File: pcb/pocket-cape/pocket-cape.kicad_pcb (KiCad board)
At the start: 2 copper layers, 49 x 32.1 mm, 29 parts, among them J1 Sync1, J10 Display, J11 USB1, J2 12..16V, J3 Sync2, J4 Sled, J5 Laser1, J6 PM1, J7 PM2, J8 Laser2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

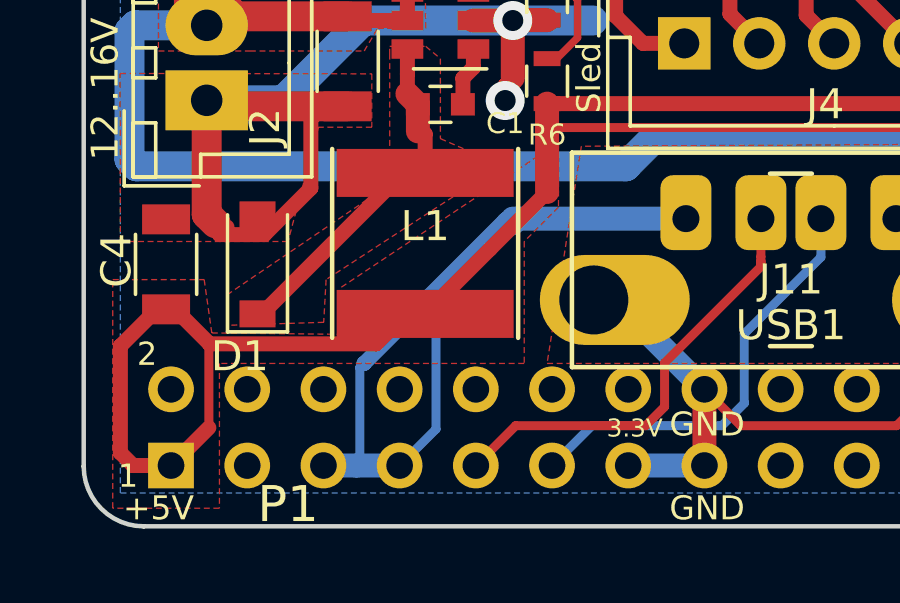
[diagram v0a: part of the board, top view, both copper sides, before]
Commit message: Update values in Schematic; directly connect USB 5V with DC/DC 5V.
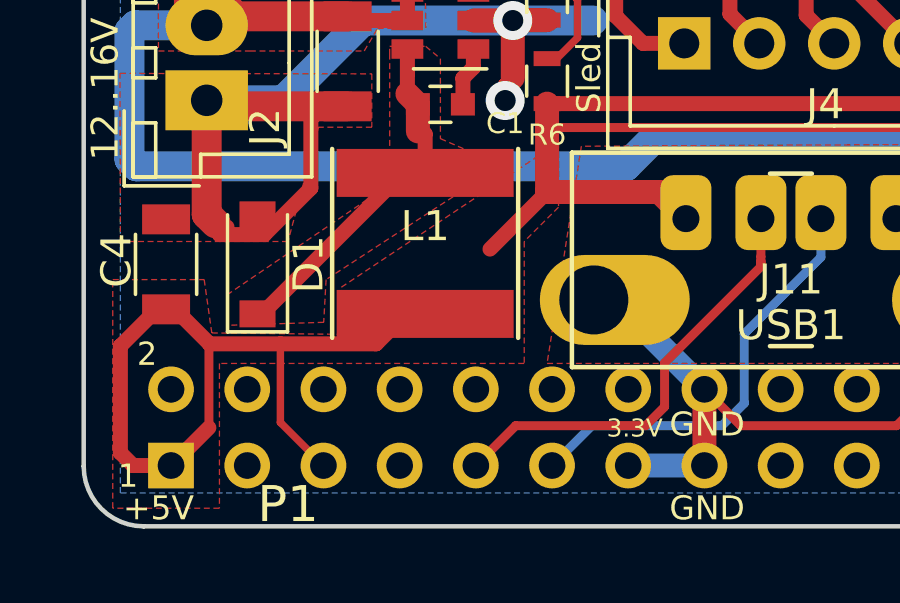
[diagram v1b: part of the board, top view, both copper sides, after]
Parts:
- D1: value D -> MBR230LSFT1G
- R6: value R -> 6k2
- R7: value R -> 1k2
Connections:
- J11 pad 1: USB_DC -> VDD_5V
- P1 pad 5: USB_DC -> VDD_5V
- P1 pad 7: USB_DC -> Net-(P1-Pad7)
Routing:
- net USB_DC: track 32.5 -> 0.00 mm
- net VDD_5V: track 83.8 -> 90.4 mm

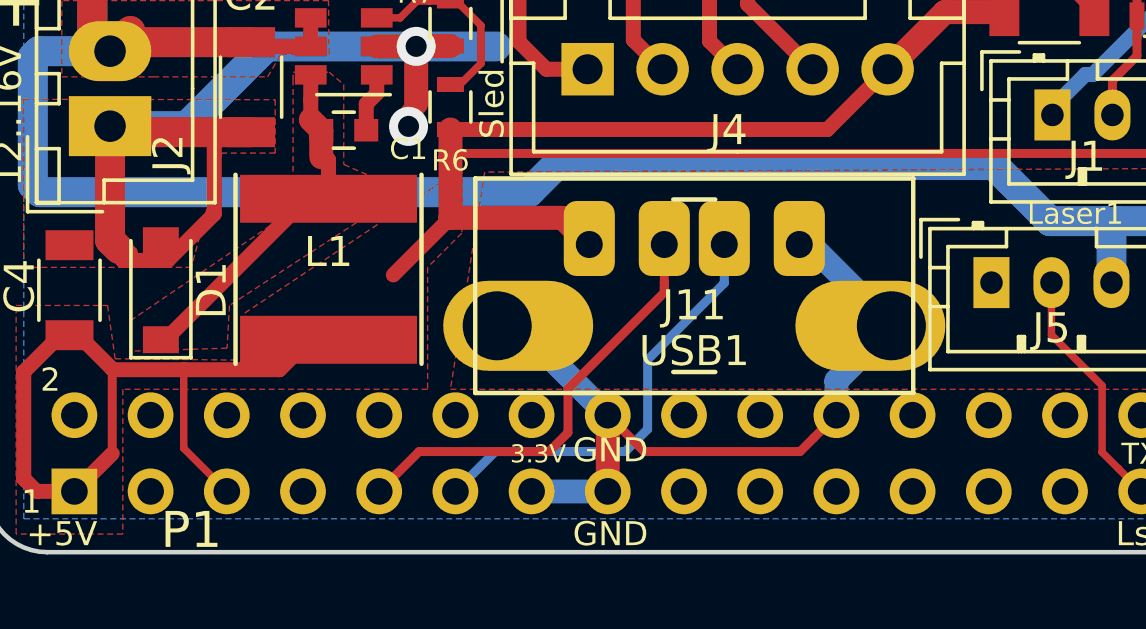
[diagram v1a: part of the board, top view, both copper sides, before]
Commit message: Connect USB output to SYS 5V
o SYS 5V has a cleaner switch-on transition than the raw DC/DC out.
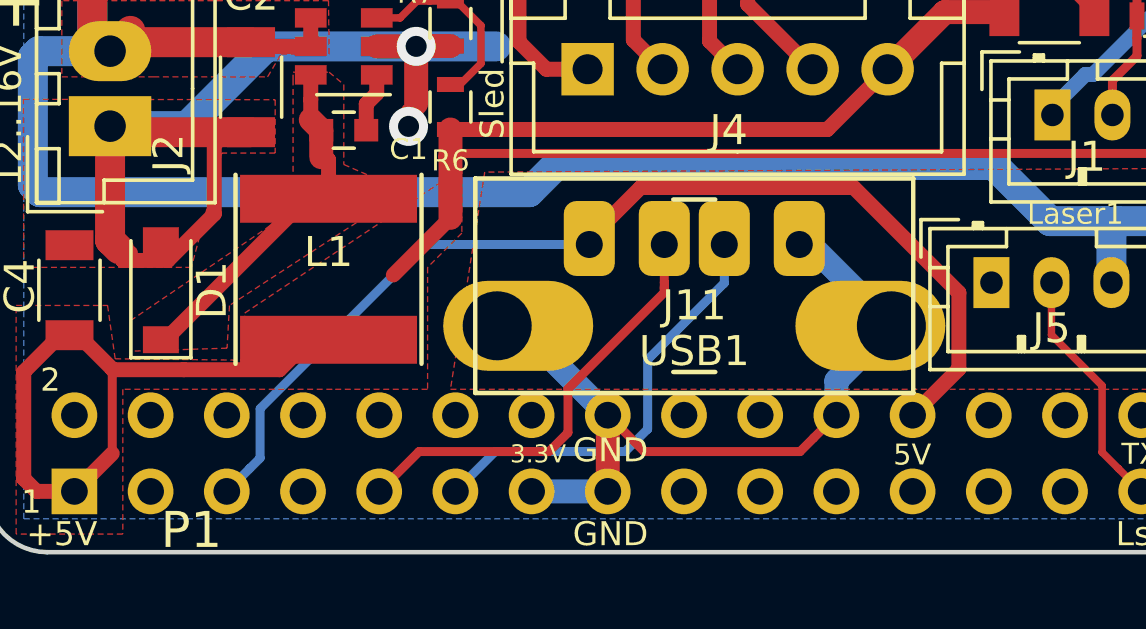
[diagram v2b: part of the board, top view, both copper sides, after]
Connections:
- J11 pad 1: VDD_5V -> SYS_VOUT
- P1 pad 24: Net-(P1-Pad24) -> SYS_VOUT
- P1 pad 5: VDD_5V -> SYS_VOUT
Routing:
- net SYS_VOUT: track 0.00 -> 35.8 mm
- net VDD_5V: track 90.4 -> 80.7 mm
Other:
- board text added: "5V"

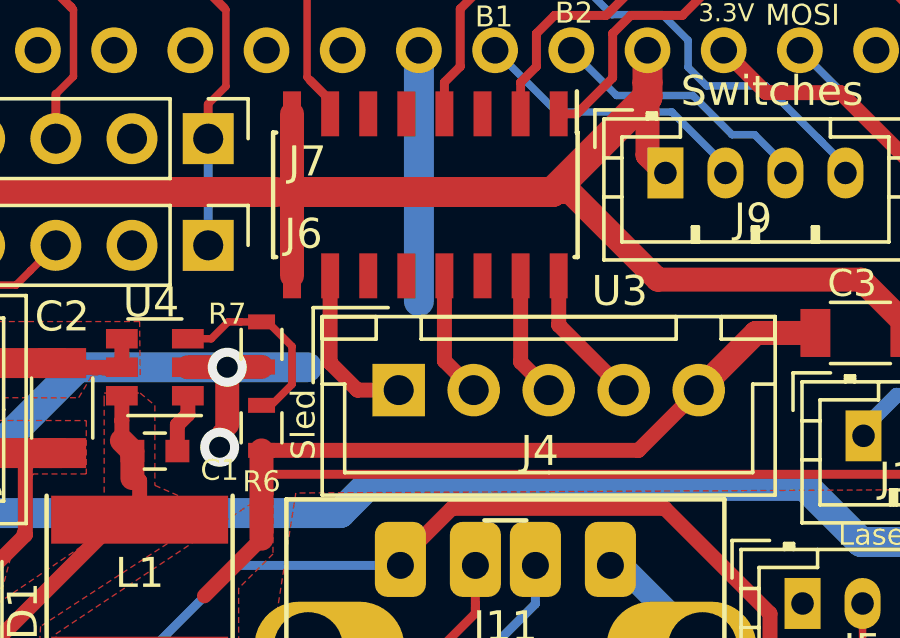
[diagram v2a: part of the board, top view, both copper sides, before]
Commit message: Connect flyback diodes to +5V.
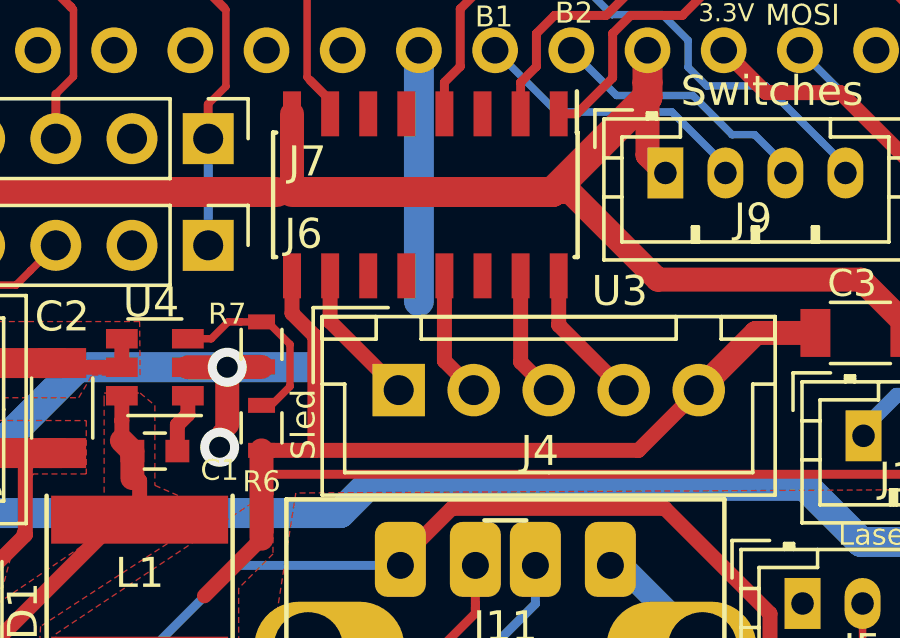
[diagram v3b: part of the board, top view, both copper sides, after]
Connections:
- U3 pad 9: GND -> VDD_5V
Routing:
- net VDD_5V: track 80.7 -> 86.9 mm
- net GND: track 145.7 -> 142.9 mm
- net Net-(J4-Pad1): track 5.56 -> 4.76 mm
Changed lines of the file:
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@@
-(kicad_pcb (version 20170922) (host pcbnew "(2017-10-06 revision d6c0d320d)-master")
+(kicad_pcb (version 20170922) (host pcbnew "(2017-10-26 revision fc5e8e5f5)-master")
 (general
   (thickness 1.6)
   (drawings 42)
-  (tracks 343)
-  (zones 0)
-  (modules 29)
-  (nets 86)
-)
-(page A4)
-(title_block
-  (title "LDGraphy PocketBeagle Cape")
-  (date 2017-09-30)
-  (comment 1 h.zeller@acm.org)
-  (comment 2 http://github.com/hzeller/ldgraphy)
-)
-(layers
-  (0 Top signal)
-  (31 Bottom signal)
-  (32 B.Adhes user hide)
-  (33 F.Adhes user hide)
-  (34 B.Paste user hide)
-  (35 F.Paste user hide)
-  (36 B.SilkS user)
-  (37 F.SilkS user)
-  (38 B.Mask user hide)
-  (39 F.Mask user hide)
-  (40 Dwgs.User user hide)
-  (41 Cmts.User user hide)
-  (42 Eco1.User user hide)
-  (43 Eco2.User user hide)
-  (44 Edge.Cuts user)
-  (45 Margin user hide)
-  (46 B.CrtYd user)
-  (47 F.CrtYd user)
-  (48 B.Fab user)
-  (49 F.Fab user)
-)
-(general
-  (thickness 1.6)
-  (drawings 42)
-  (tracks 343)
+  (tracks 345)
   (zones 0)
   (modules 29)
@@
 )
 (setup
-  (last_trace_width 0.25)
+  (last_trace_width 0.5)
   (user_trace_width 0.25)
   (user_trace_width 0.3)
@@
       (net 1 GND))
     (pad 9 smd rect (at 2.7 4.445 270) (size 1.5 0.6) (layers Top F.Paste F.Mask)
-      (net 1 GND))
+      (net 2 VDD_5V))
     (pad 10 smd rect (at 2.7 3.175 270) (size 1.5 0.6) (layers Top F.Paste F.Mask)
       (net 6 "Net-(J4-Pad1)"))
@@
   (segment (start 152.3111 116.4336) (end 152.3111 115.2869) (width 0.8) (layer Bottom) (net 1))
   (segment (start 152.3111 115.2869) (end 154.144 113.454) (width 0.8) (layer Bottom) (net 1))
-  (segment (start 140.462 98.298) (end 140.462 101.092) (width 0.8) (layer Top) (net 1))
   (segment (start 140.462 95.692) (end 140.462 98.298) (width 0.8) (layer Top) (net 1))
   (segment (start 140.462 98.298) (end 149.146002 98.298) (width 1) (layer Top) (net 1))
@@
   (segment (start 168.77 97.2775) (end 168.77 96.71) (width 0.25) (layer Top) (net 1))
   (segment (start 144.812 116.3127) (end 144.6911 116.4336) (width 0.8) (layer Top) (net 1))
+  (segment (start 141.224 106.91) (end 152.01 106.91) (width 0.5) (layer Top) (net 2))
+  (segment (start 139.446 106.91) (end 141.224 106.91) (width 0.5) (layer Top) (net 2))
+  (segment (start 140.462 101.092) (end 140.462 102.342) (width 0.5) (layer Top) (net 2))
+  (segment (start 140.462 102.342) (end 141.224 103.104) (width 0.5) (layer Top) (net 2))
+  (segment (start 141.224 103.104) (end 141.224 106.91) (width 0.5) (layer Top) (net 2))
   (segment (start 130.556 114.918001) (end 133.747999 114.918001) (width 0.5) (layer Top) (net 2))
   (segment (start 128.196001 114.918001) (end 130.556 114.918001) (width 0.5) (layer Top) (net 2))
@@
   (segment (start 163.421001 107.707999) (end 164.171 106.958) (width 0.3) (layer Top) (net 2))
   (segment (start 164.171 106.958) (end 164.846 106.958) (width 0.3) (layer Top) (net 2))
-  (segment (start 139.446 106.91) (end 152.01 106.91) (width 0.5) (layer Top) (net 2))
   (segment (start 152.01 106.91) (end 154.018 104.902) (width 0.5) (layer Top) (net 2))
   (segment (start 139.446 109.856) (end 137.542 111.76) (width 0.5) (layer Top) (net 2))
@@
   (segment (start 134.79 104.14) (end 132.31 104.14) (width 0.5) (layer Top) (net 5))
   (segment (start 132.31 104.14) (end 132.08 103.91) (width 0.5) (layer Top) (net 5))
-  (segment (start 141.732 101.092) (end 141.732 103.991) (width 0.5) (layer Top) (net 6))
-  (segment (start 141.732 103.991) (end 142.643 104.902) (width 0.5) (layer Top) (net 6))
-  (segment (start 142.643 104.902) (end 144.018 104.902) (width 0.5) (layer Top) (net 6))
+  (segment (start 141.732 102.616) (end 144.018 104.902) (width 0.5) (layer Top) (net 6))
+  (segment (start 141.732 101.092) (end 141.732 102.616) (width 0.5) (layer Top) (net 6))
   (segment (start 145.542 101.092) (end 145.542 103.926) (width 0.5) (layer Top) (net 7))
   (segment (start 145.542 103.926) (end 146.518 104.902) (width 0.5) (layer Top) (net 7))
@@
   (segment (start 135.297 107.835) (end 135.382 107.92) (width 0.5) (layer Top) (net 16))
   (segment (start 135.382 107.92) (end 135.382 109.22) (width 0.5) (layer Top) (net 16))
+  (segment (start 139.765 105.41) (end 140.394989 104.780011) (width 0.25) (layer Top) (net 17))
+  (segment (start 139.646 102.628) (end 139.446 102.628) (width 0.25) (layer Top) (net 17))
+  (segment (start 140.394989 104.780011) (end 140.394989 103.376989) (width 0.25) (layer Top) (net 17))
+  (segment (start 140.394989 103.376989) (end 139.646 102.628) (width 0.25) (layer Top) (net 17))
   (segment (start 148.082 101.092) (end 148.082 103.966) (width 0.5) (layer Top) (net 18))
   (segment (start 148.082 103.966) (end 149.018 104.902) (width 0.5) (layer Top) (net 18))
@@
   (segment (start 135.14 106.934) (end 135.14 107.835) (width 0.8) (layer Top) (net 16))
   (segment (start 134.79 106.584) (end 135.14 106.934) (width 0.8) (layer Top) (net 16))
-  (segment (start 140.462 104.713) (end 140.462 103.444) (width 0.25) (layer Top) (net 17))
-  (segment (start 140.462 103.444) (end 139.646 102.628) (width 0.25) (layer Top) (net 17))
-  (segment (start 139.646 102.628) (end 139.446 102.628) (width 0.25) (layer Top) (net 17))
-  (segment (start 139.765 105.41) (end 140.462 104.713) (width 0.25) (layer Top) (net 17))
   (segment (start 136.99 103.19) (end 137.77 103.19) (width 0.25) (layer Top) (net 17))
   (segment (start 137.77 103.19) (end 138.332 102.628) (width 0.25) (layer Top) (net 17))

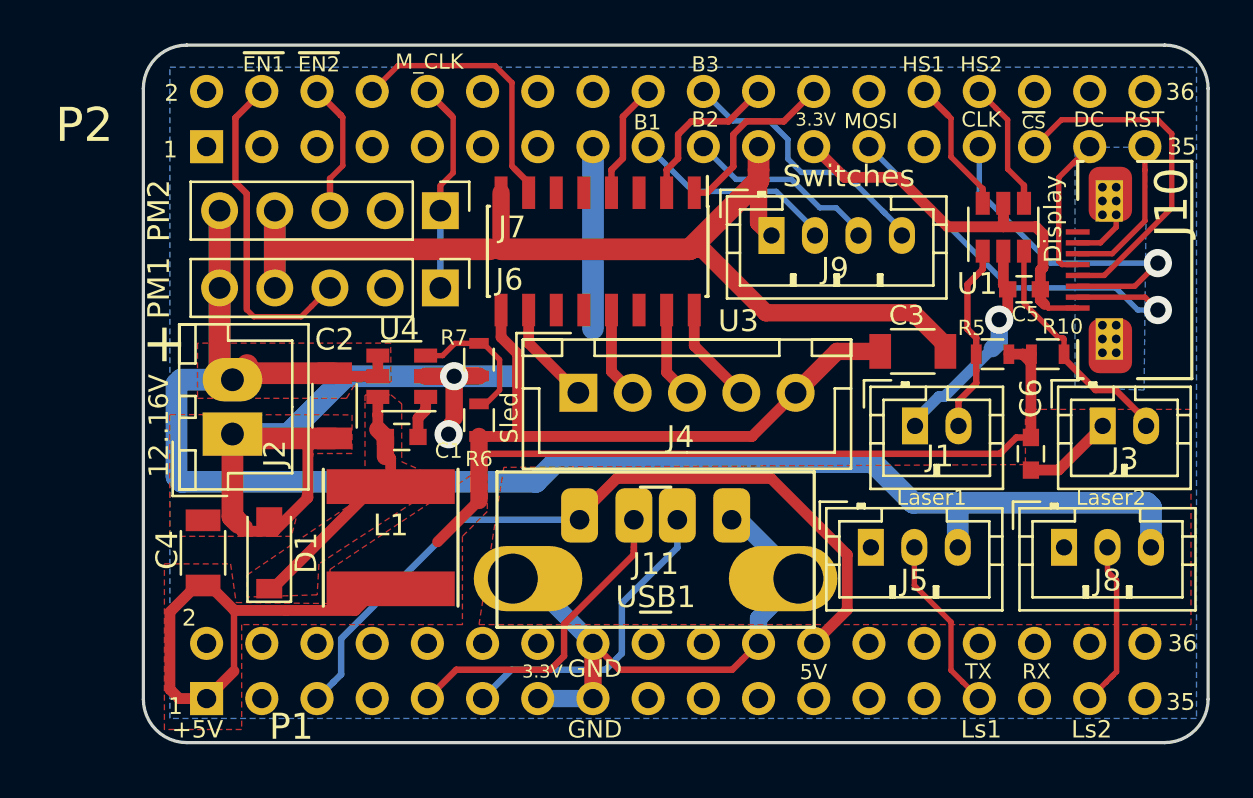
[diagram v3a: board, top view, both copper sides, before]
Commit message: Label motor phases on GPIO header for easier measurements.
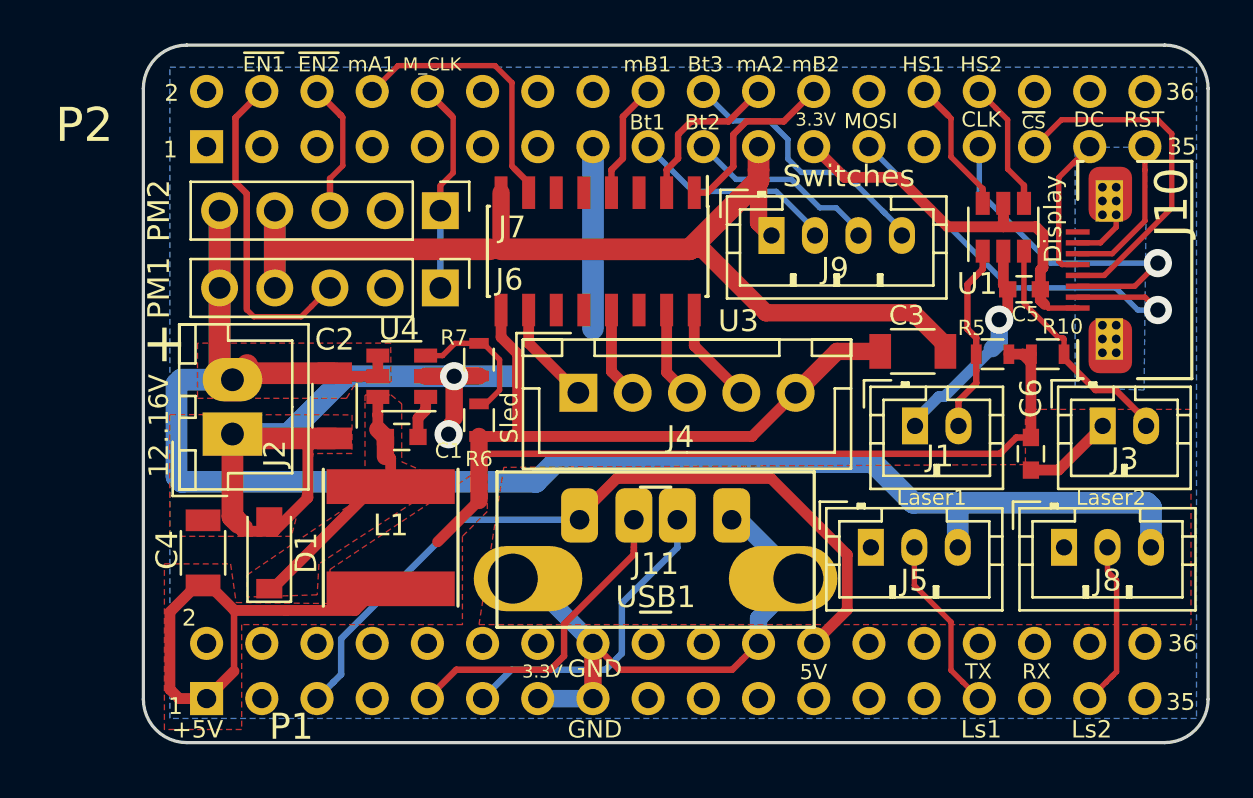
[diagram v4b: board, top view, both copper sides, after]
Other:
- board text added: "Bt1"
- board text added: "Bt2"
- board text added: "Bt3"
- board text added: "mA1"
- board text added: "mA2"
- board text added: "mB1"
- board text added: "mB2"
- board text removed: "B1"
- board text removed: "B2"
- board text removed: "B3"
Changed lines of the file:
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@@
 (general
   (thickness 1.6)
-  (drawings 42)
+  (drawings 46)
   (tracks 345)
   (zones 0)
@@
 )
 (setup
-  (last_trace_width 0.5)
+  (last_trace_width 0.25)
   (user_trace_width 0.25)
   (user_trace_width 0.3)
@@
     )
   )
+  (gr_text mB1 (at 147.193 89.789) (layer F.SilkS)
+    (effects (font (size 0.7 0.7) (thickness 0.12)))
+  )
+  (gr_text mB2 (at 154.94 89.789) (layer F.SilkS)
+    (effects (font (size 0.7 0.7) (thickness 0.12)))
+  )
+  (gr_text mA2 (at 152.4 89.789) (layer F.SilkS)
+    (effects (font (size 0.7 0.7) (thickness 0.12)))
+  )
+  (gr_text mA1 (at 134.493 89.789) (layer F.SilkS)
+    (effects (font (size 0.7 0.7) (thickness 0.12)))
+  )
   (gr_text 5V (at 154.8384 117.7544) (layer F.SilkS)
     (effects (font (size 0.7 0.7) (thickness 0.12)))
@@
     (effects (font (size 0.7 0.7) (thickness 0.12)))
   )
-  (gr_text B1 (at 147.193 92.456) (layer F.SilkS)
-    (effects (font (size 0.7 0.7) (thickness 0.15)))
-  )
-  (gr_text B2 (at 149.86 92.329) (layer F.SilkS)
-    (effects (font (size 0.7 0.7) (thickness 0.15)))
-  )
-  (gr_text B3 (at 149.86 89.789) (layer F.SilkS)
-    (effects (font (size 0.7 0.7) (thickness 0.15)))
+  (gr_text Bt1 (at 147.193 92.456) (layer F.SilkS)
+    (effects (font (size 0.7 0.7) (thickness 0.12)))
+  )
+  (gr_text Bt2 (at 149.733 92.456) (layer F.SilkS)
+    (effects (font (size 0.7 0.7) (thickness 0.12)))
+  )
+  (gr_text Bt3 (at 149.86 89.789) (layer F.SilkS)
+    (effects (font (size 0.7 0.7) (thickness 0.12)))
   )
   (gr_arc (start 171 90.9) (end 173 90.9) (angle -90) (layer Edge.Cuts) (width 0.15))
@@
   )
   (gr_text ~EN1 (at 129.54 89.789) (layer F.SilkS)
-    (effects (font (size 0.7 0.7) (thickness 0.15)))
+    (effects (font (size 0.7 0.7) (thickness 0.12)))
   )
   (gr_text ~EN2 (at 132.08 89.789) (layer F.SilkS)
-    (effects (font (size 0.7 0.7) (thickness 0.15)))
-  )
-  (gr_text M_CLK (at 137.16 89.662) (layer F.SilkS)
-    (effects (font (size 0.7 0.7) (thickness 0.15)))
+    (effects (font (size 0.7 0.7) (thickness 0.12)))
+  )
+  (gr_text M_CLK (at 137.287 89.789) (layer F.SilkS)
+    (effects (font (size 0.6 0.6) (thickness 0.12)))
   )
   (gr_text "Ls2\n" (at 167.64 120.396) (layer F.SilkS)
-    (effects (font (size 0.8 0.8) (thickness 0.15)))
+    (effects (font (size 0.8 0.8) (thickness 0.12)))
   )
   (gr_text Ls1 (at 162.56 120.396) (layer F.SilkS)
-    (effects (font (size 0.8 0.8) (thickness 0.15)))
+    (effects (font (size 0.8 0.8) (thickness 0.12)))
   )
   (gr_text GND (at 144.78 117.602) (layer F.SilkS)
-    (effects (font (size 0.8 0.8) (thickness 0.15)))
+    (effects (font (size 0.8 0.8) (thickness 0.12)))
   )
   (gr_text HS1 (at 159.893 89.789) (layer F.SilkS)
-    (effects (font (size 0.7 0.7) (thickness 0.15)))
+    (effects (font (size 0.7 0.7) (thickness 0.12)))
   )
   (gr_text HS2 (at 162.56 89.789) (layer F.SilkS)
-    (effects (font (size 0.7 0.7) (thickness 0.15)))
+    (effects (font (size 0.7 0.7) (thickness 0.12)))
   )
   (gr_text +5V (at 126.492 120.396) (layer F.SilkS)
-    (effects (font (size 0.8 0.8) (thickness 0.15)))
+    (effects (font (size 0.8 0.8) (thickness 0.12)))
   )
   (gr_text GND (at 144.78 120.396) (layer F.SilkS)
-    (effects (font (size 0.8 0.8) (thickness 0.15)))
+    (effects (font (size 0.8 0.8) (thickness 0.12)))
   )
   (gr_text %%gitversion%% (at 156.718 107.442) (layer B.SilkS)
